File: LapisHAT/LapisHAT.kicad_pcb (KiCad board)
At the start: 4 copper layers, 53 parts, among them J1 Conn_01x02, J10 Conn_01x02, J11 Conn_01x02, J12 Conn_01x02, J13 Conn_01x03, J14 Conn_01x03, J15 Conn_01x03, J16 Conn_01x03, J17 Conn_01x02, J18 Conn_01x02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

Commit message: Initial schematic
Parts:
- added C18: 47u, Capacitor_SMD:C_0805_2012Metric, F.Cu at (61.5, 39.4)
- added C19: 100n, Capacitor_SMD:C_0603_1608Metric, F.Cu at (66.2, 39.6)
- added C20: 100n, Capacitor_SMD:C_0603_1608Metric, F.Cu at (63.4, 39.6)
- added C21: 47u, Capacitor_SMD:C_0805_2012Metric, F.Cu at (66.2, 32.5)
- added C22: 100n, Capacitor_SMD:C_0603_1608Metric, F.Cu at (71.1, 32.5)
- added C23: 100n, Capacitor_SMD:C_0603_1608Metric, F.Cu at (69.4, 32.5)
- added J19: Conn_01x02, Connector_PinHeader_2.54mm:PinHeader_1x02_P2.54mm_Vertical, F.Cu at (59.9, 32.4)
- added R7: 10k, Resistor_SMD:R_0603_1608Metric, F.Cu at (65.4, 46.7)
- added R8: 10k, Resistor_SMD:R_0603_1608Metric, F.Cu at (71.0, 39.8)
- added U10: DRV8231ADSG, Package_SON:WSON-8-1EP_2x2mm_P0.5mm_EP0.9x1.6mm, F.Cu at (65.2, 43.2)
- added U11: DRV8231ADSG, Package_SON:WSON-8-1EP_2x2mm_P0.5mm_EP0.9x1.6mm, F.Cu at (70.9, 36.3)
- J2: moved to B.Cu
- J3, J4: value Conn_01x07 -> Conn_01x06; footprint Connector_PinHeader_2.54mm:PinHeader_1x07_P2.54mm_Vertical -> Connector_PinHeader_2.54mm:PinHeader_1x06_P2.54mm_Vertical
- moved C8 174.8 mm to (61.5, 58.1), turned to 180 degrees
- moved J18 173.9 mm to (59.3, 72.7), turned to 90 degrees
- moved U6 170.8 mm to (66.0, 61.4), turned to 180 degrees
- moved Q1 169.1 mm to (65.8, 68.4), turned to 180 degrees
- moved Q2 169.0 mm to (65.9, 72.7), turned to 180 degrees
- moved J17 168.8 mm to (59.2, 68.4), turned to 90 degrees
- moved C5 168.3 mm to (67.9, 49.1), turned to 90 degrees
- moved C10 166.1 mm to (64.8, 57.5), turned to 90 degrees
- moved U4 165.9 mm to (70.5, 52.8), turned to 180 degrees
- moved R2 164.7 mm to (66.2, 63.5), turned to 180 degrees
- moved C9 164.3 mm to (66.5, 57.6), turned to 90 degrees
- moved J4 163.5 mm to (54.6, 47.4)
- moved J9 163.4 mm to (72.5, 79.8), turned to 90 degrees
- moved C7 162.4 mm to (68.2, 58.1), turned to 90 degrees
- moved C2 161.2 mm to (67.8, 39.6), turned to 90 degrees
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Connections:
- net Net-(J5-Pin_1) renamed /Tooling/MOTOR2_OUT1
- net Net-(J5-Pin_2) renamed /Tooling/MOTOR2_OUT2
- net Net-(J6-Pin_1) renamed /Tooling/MOTOR3_OUT1
- net Net-(J6-Pin_2) renamed /Tooling/MOTOR3_OUT2
- A1 pad 1: /Pico/MOTOR0_PWM -> /Pico/MOTOR0_DIR
- A1 pad 10: /Pico/ESC3 -> /Pico/MOTOR3_PWM
- A1 pad 11: /Pico/ESC4 -> /Pico/LED0
- A1 pad 12: /Pico/ESC5 -> /Pico/LED1
- A1 pad 14: /Pico/SERVO0 -> /Pico/ESC0
- A1 pad 15: /Pico/SERVO1 -> /Pico/ESC1
- A1 pad 16: /Pico/SERVO2 -> /Pico/ESC2
- A1 pad 17: /Pico/SERVO3 -> /Pico/ESC3
- A1 pad 19: /Pico/LED0 -> /Pico/ESC4
- A1 pad 2: /Pico/MOTOR0_DIR -> /Pico/MOTOR1_DIR
- A1 pad 20: /Pico/LED1 -> /Pico/ESC5
- A1 pad 21: /Pico/MOTOR2_DIR -> /Pico/SERVO0
- A1 pad 22: /Pico/MOTOR2_PWM -> /Pico/SERVO1
- A1 pad 24: /Pico/MOTOR1_PWM -> /Pico/SERVO2
- A1 pad 25: /Pico/MOTOR1_DIR -> /Pico/SERVO3
- A1 pad 4: /Pico/MOTOR3_DIR -> /Pico/MOTOR2_DIR
- A1 pad 5: /Pico/MOTOR3_PWM -> /Pico/MOTOR3_DIR
- A1 pad 6: /Pico/ESC0 -> /Pico/MOTOR0_PWM
- A1 pad 7: /Pico/ESC1 -> /Pico/MOTOR1_PWM
- A1 pad 9: /Pico/ESC2 -> /Pico/MOTOR2_PWM
- J3 pad 1: +12V -> +3V3
- J3 pad 2: +3V3 -> /Tooling/MOTOR0_OUT1
- J3 pad 3: Net-(J3-Pin_3) -> /Tooling/MOTOR0_OUT2
- J3 pad 4: Net-(J3-Pin_4) -> /I2C/ENCODER0_SDA
- J3 pad 5: /I2C/ENCODER0_SDA -> /I2C/ENCODER0_SCL
- J3 pad 6: /I2C/ENCODER0_SCL -> GND
- J4 pad 1: +12V -> +3V3
- J4 pad 2: +3V3 -> /Tooling/MOTOR1_OUT1
- J4 pad 3: Net-(J4-Pin_3) -> /Tooling/MOTOR1_OUT2
- J4 pad 4: Net-(J4-Pin_4) -> /I2C/ENCODER1_SDA
- J4 pad 5: /I2C/ENCODER1_SDA -> /I2C/ENCODER1_SCL
- J4 pad 6: /I2C/ENCODER1_SCL -> GND
- U1 pad 4: Net-(J3-Pin_4) -> Net-(U1-Y1)
- U1 pad 6: Net-(J3-Pin_3) -> Net-(U1-Y0)
- U2 pad 4: Net-(J4-Pin_4) -> Net-(U10-IN2)
- U2 pad 6: Net-(J4-Pin_3) -> Net-(U10-IN1)
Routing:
- net /I2C/ENCODER0_SCL: track 0.00 -> 75.0 mm, vias 0 -> 1
- net /I2C/ENCODER0_SDA: track 0.00 -> 71.6 mm, vias 0 -> 2
- net /I2C/ENCODER1_SCL: track 0.00 -> 69.4 mm, vias 0 -> 2
- net /I2C/ENCODER1_SDA: track 0.00 -> 66.3 mm, vias 0 -> 1
- net +3V3: track 0.00 -> 39.7 mm, vias 0 -> 13
- net +5V: track 0.00 -> 29.8 mm
- net /I2C/ENCODER_SDA: track 0.00 -> 24.3 mm
- net +12V: track 0.00 -> 23.6 mm, vias 0 -> 12
- net /I2C/ENCODER_SCL: track 0.00 -> 23.2 mm
- net GND: track 0.00 -> 20.1 mm, vias 0 -> 16
- net /Pico/MOTOR3_DIR: track 0.00 -> 19.7 mm
- net /Pico/MOTOR0_PWM: track 0.00 -> 18.3 mm, vias 0 -> 1
- net /Pico/LED1: track 0.00 -> 18.3 mm
- net /Pico/LED0: track 0.00 -> 17.5 mm
- net /Pico/MOTOR1_PWM: track 0.00 -> 16.7 mm, vias 0 -> 1
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- added copper zone on In2.Cu, net +12V
- added copper zone on In1.Cu, net +3V3
- added copper zone on In1.Cu, net +5V
- added copper zone on In1.Cu, net /Tooling/MOTOR0_OUT1
- added copper zone on In1.Cu, net /Tooling/MOTOR0_OUT2
- added copper zone on In1.Cu, net /Tooling/MOTOR1_OUT1
- added copper zone on In1.Cu, net /Tooling/MOTOR1_OUT2
- added copper zone on In1.Cu, net /Tooling/MOTOR2_OUT1
- added copper zone on In1.Cu, net /Tooling/MOTOR2_OUT2
- added copper zone on In1.Cu, net /Tooling/MOTOR3_OUT1
- added copper zone on In1.Cu, net /Tooling/MOTOR3_OUT2
- added copper zone on B.Cu, net GND
- added copper zone on F.Cu, net GND

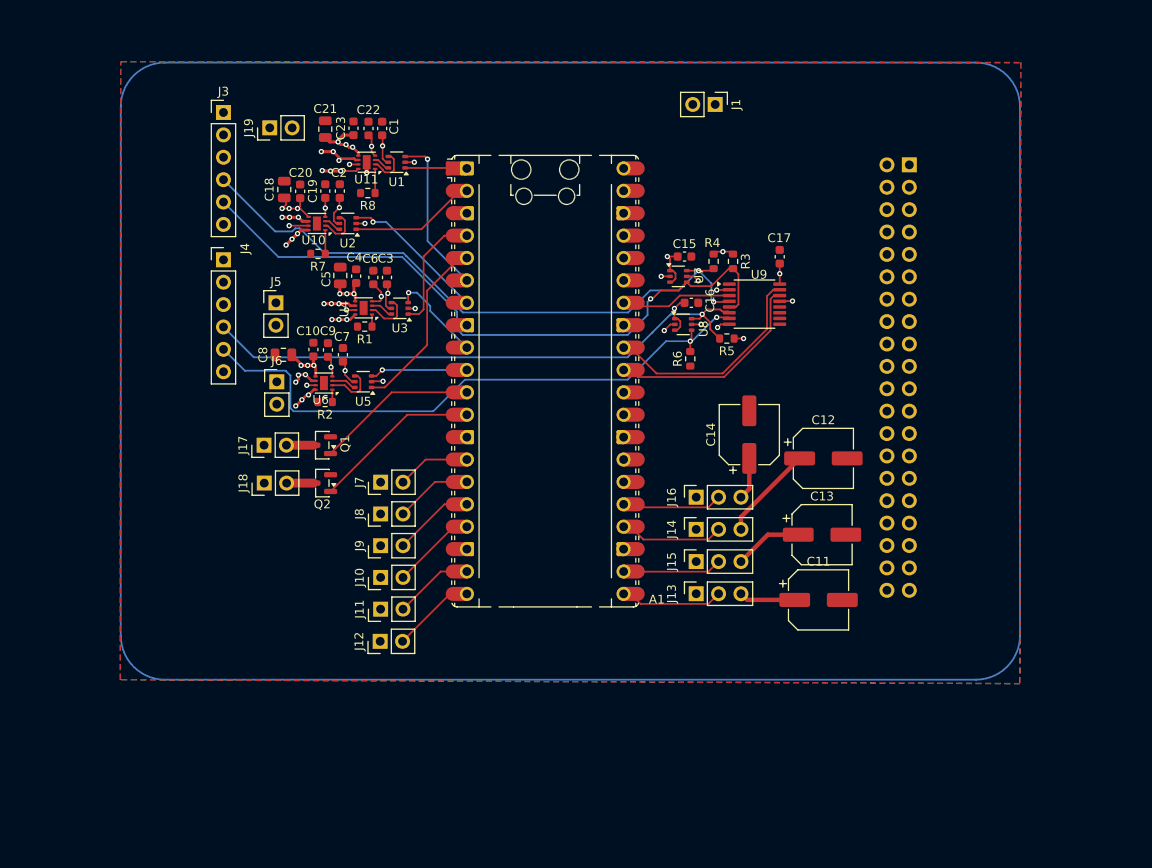
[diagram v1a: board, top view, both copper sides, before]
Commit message: New Lapis Hat
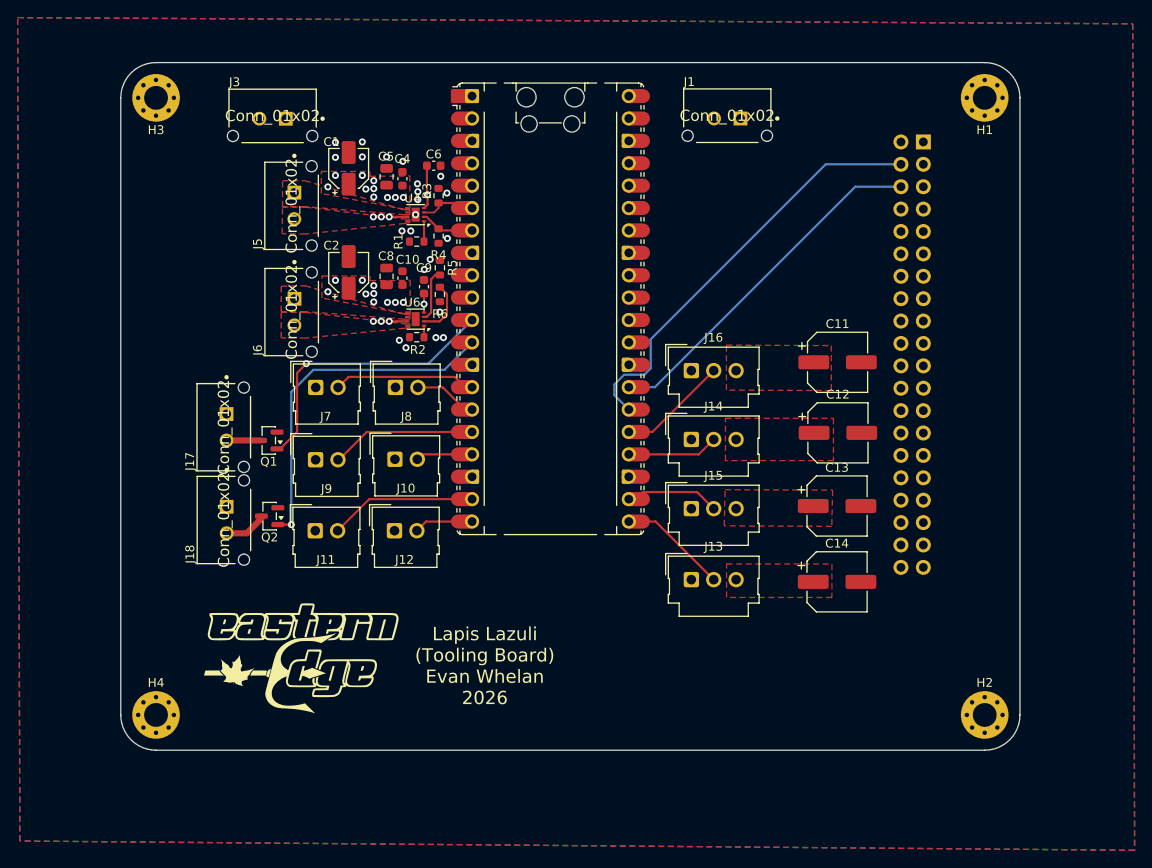
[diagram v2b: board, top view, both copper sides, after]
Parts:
- removed C15, C16: 10n, Capacitor_SMD:C_0603_1608Metric
- removed C17, C19, C20, C22, C23, C3, C7: 100n, Capacitor_SMD:C_0603_1608Metric
- removed C18, C21: 47u, Capacitor_SMD:C_0805_2012Metric
- removed J19: Conn_01x02, Connector_PinHeader_2.54mm:PinHeader_1x02_P2.54mm_Vertical
- removed J4: Conn_01x06, Connector_PinHeader_2.54mm:PinHeader_1x06_P2.54mm_Vertical
- removed R7, R8: 10k, Resistor_SMD:R_0603_1608Metric
- removed U1, U2, U3, U5: NC7SZ18P6X, Package_TO_SOT_SMD:SOT-363_SC-70-6
- removed U10, U11: DRV8231ADSG, Package_SON:WSON-8-1EP_2x2mm_P0.5mm_EP0.9x1.6mm
- removed U7, U8: LTC4311CSC6-TRPBF, Package_TO_SOT_SMD:SOT-363_SC-70-6
- removed U9: TCA9546APW, Package_SO:TSSOP-16_4.4x5mm_P0.65mm
- added G***: LOGO, EER_Logos:eer_logo_small, F.Cu at (63.5, 91.3)
- added H1: MountingHole_Pad, MountingHole:MountingHole_2.7mm_M2.5_Pad_Via, F.Cu at (141.0, 29.0)
- added H2: MountingHole_Pad, MountingHole:MountingHole_2.7mm_M2.5_Pad_Via, F.Cu at (141.0, 99.0)
- added H3: MountingHole_Pad, MountingHole:MountingHole_2.7mm_M2.5_Pad_Via, F.Cu at (47.0, 29.0)
- added H4: MountingHole_Pad, MountingHole:MountingHole_2.7mm_M2.5_Pad_Via, F.Cu at (47.0, 99.0)
- C1, C2: value 100n -> 10u; footprint Capacitor_SMD:C_0603_1608Metric -> Capacitor_SMD:CP_Elec_4x5.4
- J1, J17, J18, J5, J6: footprint Connector_PinHeader_2.54mm:PinHeader_1x02_P2.54mm_Vertical -> footprints:Molex-43650-0227_-MFG
- J10, J11, J12, J7, J8, J9: footprint Connector_PinHeader_2.54mm:PinHeader_1x02_P2.54mm_Vertical -> Connector_Molex:Molex_SL_171971-0002_1x02_P2.54mm_Vertical
- J13, J14, J15, J16: footprint Connector_PinSocket_2.54mm:PinSocket_1x03_P2.54mm_Vertical -> Connector_Molex:Molex_SL_171971-0003_1x03_P2.54mm_Vertical
- J3: value Conn_01x06 -> Conn_01x02; footprint Connector_PinHeader_2.54mm:PinHeader_1x06_P2.54mm_Vertical -> footprints:Molex-43650-0227_-MFG
- moved R3 34.2 mm to (79.0, 40.1)
- moved R5 33.5 mm to (79.2, 48.3), turned to -90 degrees
- moved R4 31.3 mm to (79.0, 44.7), turned to 90 degrees
- moved R6 29.3 mm to (79.2, 51.3)
- moved C11 27.0 mm to (124.3, 59.0)
- moved C14 19.4 mm to (124.2, 83.9), turned to 0 degrees
- moved C8 14.7 mm to (73.2, 49.2), turned to 90 degrees
- moved J8 14.4 mm to (74.2, 61.9), turned to 0 degrees
- moved C6 14.4 mm to (78.5, 36.7), turned to 0 degrees
- moved J16 14.4 mm to (107.7, 59.9), turned to 0 degrees
- moved J10 13.5 mm to (74.1, 70.0), turned to 0 degrees
- moved C9 13.0 mm to (77.4, 50.4)
- moved J7 13.0 mm to (65.1, 61.9), turned to 0 degrees
- moved C10 12.9 mm to (75.0, 49.5)
- moved R2 12.7 mm to (76.6, 56.1)
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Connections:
- A1 pad 1: /Pico/MOTOR0_DIR -> unconnected-(A1-GPIO0-Pad1)
- A1 pad 10: /Pico/MOTOR3_PWM -> /Pico/MOTOR1_IN2
- A1 pad 2: /Pico/MOTOR1_DIR -> unconnected-(A1-GPIO1-Pad2)
- A1 pad 31: /I2C/ENCODER_SCL -> unconnected-(A1-GPIO26_ADC0-Pad31)_1
- A1 pad 32: /I2C/ENCODER_SDA -> unconnected-(A1-GPIO27_ADC1-Pad32)
- A1 pad 34: /I2C/~{I2C_MUX_RESET} -> unconnected-(A1-GPIO28_ADC2-Pad34)
- A1 pad 4: /Pico/MOTOR2_DIR -> unconnected-(A1-GPIO2-Pad4)_1
- A1 pad 5: /Pico/MOTOR3_DIR -> unconnected-(A1-GPIO3-Pad5)_1
- A1 pad 6: /Pico/MOTOR0_PWM -> /Pico/MOTOR0_IN1
- A1 pad 7: /Pico/MOTOR1_PWM -> /Pico/MOTOR0_IN2
- A1 pad 9: /Pico/MOTOR2_PWM -> /Pico/MOTOR1_IN1
- C1 pad 1: +3V3 -> +12V
- C2 pad 1: +3V3 -> +12V
- J3 pad 1: +3V3 -> GND
- J3 pad 2: /Tooling/MOTOR0_OUT1 -> +12V
- J5 pad 1: /Tooling/MOTOR2_OUT1 -> /Tooling/MOTOR0_OUT1
- J5 pad 2: /Tooling/MOTOR2_OUT2 -> /Tooling/MOTOR0_OUT2
- J6 pad 1: /Tooling/MOTOR3_OUT1 -> /Tooling/MOTOR0_OUT1
- J6 pad 2: /Tooling/MOTOR3_OUT2 -> /Tooling/MOTOR0_OUT2
- R3 pad 1: +3V3 -> GND
- R3 pad 2: /I2C/ENCODER0_SCL -> /Pico/MOTOR0_IN1
- R4 pad 1: +3V3 -> GND
- R4 pad 2: /I2C/ENCODER0_SDA -> /Pico/MOTOR0_IN2
- R5 pad 1: +3V3 -> GND
- R5 pad 2: /I2C/ENCODER1_SDA -> /Pico/MOTOR1_IN1
- R6 pad 1: +3V3 -> GND
- R6 pad 2: /I2C/ENCODER1_SCL -> /Pico/MOTOR1_IN2
- U4 pad 2: Net-(U3-Y1) -> /Pico/MOTOR0_IN2
- U4 pad 3: Net-(U3-Y0) -> /Pico/MOTOR0_IN1
- U4 pad 6: /Tooling/MOTOR2_OUT1 -> /Tooling/MOTOR0_OUT1
- U4 pad 8: /Tooling/MOTOR2_OUT2 -> /Tooling/MOTOR0_OUT2
- U6 pad 2: Net-(U5-Y1) -> /Pico/MOTOR1_IN2
- U6 pad 3: Net-(U5-Y0) -> /Pico/MOTOR1_IN1
- U6 pad 6: /Tooling/MOTOR3_OUT1 -> /Tooling/MOTOR0_OUT1
- U6 pad 8: /Tooling/MOTOR3_OUT2 -> /Tooling/MOTOR0_OUT2
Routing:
- net /I2C/ENCODER0_SCL: track 75.0 -> 0.00 mm, vias 1 -> 0
- net /I2C/ENCODER0_SDA: track 71.6 -> 0.00 mm, vias 2 -> 0
- net /I2C/ENCODER1_SCL: track 69.4 -> 0.00 mm, vias 2 -> 0
- net /I2C/ENCODER1_SDA: track 66.3 -> 0.00 mm, vias 1 -> 0
- net /Pico/PI_SDA: track 0.00 -> 48.7 mm
- net /Pico/PI_SCL: track 0.00 -> 40.3 mm
- net +3V3: track 39.7 -> 7.15 mm, vias 13 -> 2
- net +5V: track 29.8 -> 0.00 mm
- net /I2C/ENCODER_SDA: track 24.3 -> 0.00 mm
- net +12V: track 23.6 -> 0.00 mm, vias 12 -> 20
- net /I2C/ENCODER_SCL: track 23.2 -> 0.00 mm
- net /Pico/LED1: track 18.3 -> 39.4 mm, vias 0 -> 1
- net /Pico/MOTOR3_DIR: track 19.7 -> 0.00 mm
- net /Pico/MOTOR0_PWM: track 18.3 -> 0.00 mm, vias 1 -> 0
- net /Pico/MOTOR1_PWM: track 16.7 -> 0.00 mm, vias 1 -> 0
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- added copper zone on F.Cu, net +12V
- added copper zone on F.Cu, net +5V
- added copper zone on F.Cu, net /Tooling/MOTOR0_OUT1
- added copper zone on F.Cu, net /Tooling/MOTOR0_OUT2
- removed copper zone on In1.Cu, net /Tooling/MOTOR0_OUT1
- removed copper zone on In1.Cu, net /Tooling/MOTOR0_OUT2
- removed copper zone on In1.Cu, net /Tooling/MOTOR1_OUT1
- removed copper zone on In1.Cu, net /Tooling/MOTOR1_OUT2
- removed copper zone on In1.Cu, net /Tooling/MOTOR2_OUT1
- removed copper zone on In1.Cu, net /Tooling/MOTOR2_OUT2
- removed copper zone on In1.Cu, net /Tooling/MOTOR3_OUT1
- removed copper zone on In1.Cu, net /Tooling/MOTOR3_OUT2
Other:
- board outline added: 102 x 78 mm
- board text added: "Lapis Lazuli (Tooling Board) Evan Whelan 2026"

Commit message: Some review changes
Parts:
- added C3: 100u, Capacitor_SMD:CP_Elec_6.3x7.7, F.Cu at (170.2, 61.3)
- added D1: LED, LED_SMD:LED_0603_1608Metric, F.Cu at (118.8, 39.0)
- added D2: LED, LED_SMD:LED_0603_1608Metric, F.Cu at (112.5, 50.0)
- added D3: LED, LED_SMD:LED_0603_1608Metric, F.Cu at (53.5, 46.0)
- added R10: 4.7k, Resistor_SMD:R_0603_1608Metric, F.Cu at (167.0, 66.6)
- added R11: 4.7k, Resistor_SMD:R_0603_1608Metric, F.Cu at (167.0, 69.2)
- added R7: 100, Resistor_SMD:R_0603_1608Metric, F.Cu at (108.3, 39.0)
- added R8: 330, Resistor_SMD:R_0603_1608Metric, F.Cu at (119.5, 50.0)
- added R9: 2k, Resistor_SMD:R_0603_1608Metric, F.Cu at (53.5, 39.8)
- added TP1: TestPoint, TestPoint:TestPoint_Pad_2.0x2.0mm, F.Cu at (48.0, 47.2)
- added TP2: TestPoint, TestPoint:TestPoint_Pad_2.0x2.0mm, F.Cu at (122.8, 31.2)
- added TP4: TestPoint, TestPoint:TestPoint_Pad_2.0x2.0mm, F.Cu at (52.0, 55.2)
- added TP5: TestPoint, TestPoint:TestPoint_Pad_2.0x2.0mm, F.Cu at (110.0, 43.8)
- added TP6: TestPoint, TestPoint:TestPoint_Pad_2.0x2.0mm, F.Cu at (105.8, 43.8)
- C1, C2: value 10u -> 330u
- H1, H2, H3, H4: footprint MountingHole:MountingHole_2.7mm_M2.5_Pad_Via -> MountingHole:MountingHole_3.2mm_M3_Pad_Via
- moved R1 103.7 mm to (179.4, 58.5), turned to 0 degrees
- moved R2 103.0 mm to (179.4, 61.0), turned to 0 degrees
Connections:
- J6 pad 1: /Tooling/MOTOR0_OUT1 -> /Tooling/MOTOR1_OUT1
- J6 pad 2: /Tooling/MOTOR0_OUT2 -> /Tooling/MOTOR1_OUT2
- R1 pad 1: Net-(U4-IPROPI) -> GND
- R1 pad 2: GND -> /Pico/LED0
- R2 pad 1: Net-(U6-IPROPI) -> GND
- R2 pad 2: GND -> /Pico/LED1
- U4 pad 1: Net-(U4-IPROPI) -> GND
- U6 pad 1: Net-(U6-IPROPI) -> GND
- U6 pad 6: /Tooling/MOTOR0_OUT1 -> /Tooling/MOTOR1_OUT1
- U6 pad 8: /Tooling/MOTOR0_OUT2 -> /Tooling/MOTOR1_OUT2
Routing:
- net /Pico/PI_SDA: track 48.7 -> 72.8 mm
- net /Pico/PI_SCL: track 40.3 -> 60.9 mm
- net Net-(D1-A): track 0.00 -> 8.81 mm
- net +3V3: track 7.15 -> 14.0 mm
- net Net-(D2-A): track 0.00 -> 5.39 mm
- net Net-(D3-A): track 0.00 -> 4.56 mm
- net +12V: track 0.00 -> 4.00 mm, vias 20 -> 22
- net +5V: track 0.00 -> 3.67 mm, vias 0 -> 2
- net /Pico/MOTOR1_IN2: track 6.32 -> 9.67 mm
- net /Pico/MOTOR1_IN1: track 5.98 -> 8.84 mm
- net GND: track 7.70 -> 10.5 mm
- net Net-(U4-IPROPI): track 2.25 -> 0.00 mm
- net Net-(U6-IPROPI): track 1.30 -> 0.00 mm
- added copper zone on F.Cu, net /Tooling/MOTOR1_OUT1
- added copper zone on F.Cu, net /Tooling/MOTOR1_OUT2

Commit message: another layout
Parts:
- removed A1: RaspberryPi_Pico, Module:RaspberryPi_Pico_Common_Unspecified
- removed G***: LOGO, EER_Logos:eer_logo_small
- removed R10, R11: 4.7k, Resistor_SMD:R_0603_1608Metric
- removed TP5, TP6: TestPoint, TestPoint:TestPoint_Pad_2.0x2.0mm
- added J19: Conn_01x20, Connector_PinHeader_2.54mm:PinHeader_1x20_P2.54mm_Vertical, B.Cu at (122.0, 44.6)
- added J4: Conn_01x20, Connector_PinHeader_2.54mm:PinHeader_1x20_P2.54mm_Vertical, B.Cu at (97.2, 44.8)
- added R12: 4.7k, Resistor_SMD:R_0603_1608Metric, F.Cu at (125.2, 57.5)
- added R13: 4.7k, Resistor_SMD:R_0603_1608Metric, F.Cu at (127.8, 57.5)
- H1, H2, H3, H4: footprint MountingHole:MountingHole_3.2mm_M3_Pad_Via -> MountingHole:MountingHole_2.7mm_M2.5_Pad_Via
- J1, J3: footprint footprints:Molex-43650-0227_-MFG -> Connector_Molex:Molex_Micro-Fit_3.0_43650-0200_1x02_P3.00mm_Horizontal
- J10, J11, J12, J7, J8, J9: footprint Connector_Molex:Molex_SL_171971-0002_1x02_P2.54mm_Vertical -> footprints:CONN_70553-xxxx_02_MOL
- J2: moved to F.Cu
- moved Q2 289.2 mm to (345.9, 119.3), turned to 0 degrees
- moved C1 163.5 mm to (223.8, 89.1), turned to 0 degrees
- moved U4 162.9 mm to (229.9, 97.0), turned to 0 degrees
- moved C2 161.7 mm to (223.8, 94.9), turned to 0 degrees
- moved U6 160.3 mm to (229.9, 100.6), turned to 0 degrees
- moved J17 151.2 mm to (205.5, 77.0), turned to 0 degrees
- moved J18 151.0 mm to (205.5, 84.3), turned to 0 degrees
- moved Q1 148.9 mm to (206.1, 95.7)
- moved R3 147.5 mm to (217.9, 89.9), turned to 0 degrees
- moved C4 147.4 mm to (213.9, 87.4), turned to 0 degrees
- moved R4 146.9 mm to (217.9, 92.4), turned to 0 degrees
- moved R5 146.4 mm to (217.9, 94.9), turned to 0 degrees
- moved C10 146.2 mm to (213.9, 94.9), turned to 0 degrees
- moved R6 146.2 mm to (217.9, 97.4), turned to 0 degrees
- moved C6 145.5 mm to (213.9, 89.9)
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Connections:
- C3 pad 2: unconnected-(C3-Pad2) -> GND
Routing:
- net /Pico/LED1: track 39.4 -> 0.00 mm, vias 1 -> 0
- net /Pico/ESC0: track 15.4 -> 51.8 mm
- net /Pico/ESC1: track 6.39 -> 41.2 mm
- net /Pico/LED0: track 32.1 -> 0.08 mm, vias 1 -> 0
- net /Pico/PI_SDA: track 72.8 -> 43.6 mm, vias 0 -> 1
- net /Pico/ESC3: track 5.73 -> 24.8 mm
- net /Pico/PI_SCL: track 60.9 -> 43.6 mm, vias 0 -> 1
- net /Pico/ESC2: track 15.7 -> 31.3 mm
- net /Pico/SERVO3: track 12.0 -> 23.3 mm
- net +3V3: track 14.0 -> 3.52 mm, vias 2 -> 3
- net /Pico/MOTOR1_IN2: track 9.67 -> 0.00 mm
- net /Pico/MOTOR1_IN1: track 8.84 -> 0.00 mm
- net /Pico/SERVO2: track 9.53 -> 17.8 mm
- net GND: track 10.5 -> 2.42 mm, vias 28 -> 2
- net /Pico/ESC5: track 5.87 -> 13.7 mm
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- added copper zone on In2.Cu, net GND
- removed copper zone on F.Cu, net +12V
- removed copper zone on In2.Cu, net +12V
- removed copper zone on F.Cu, net +5V
- removed copper zone on F.Cu, net /Tooling/MOTOR0_OUT1
- removed copper zone on F.Cu, net /Tooling/MOTOR0_OUT2
- removed copper zone on F.Cu, net /Tooling/MOTOR1_OUT1
- removed copper zone on F.Cu, net /Tooling/MOTOR1_OUT2
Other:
- board outline removed
- board text removed: "Lapis Lazuli (Tooling Board) Evan Whelan 2026"

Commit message: Move connectors and add correct 5v cap
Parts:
- C3: value 100u -> 120u; footprint Capacitor_SMD:CP_Elec_6.3x7.7 -> Capacitor_SMD:CP_Elec_10x12.5
- moved Q2 116.1 mm to (235.4, 83.7)
- moved J7 87.7 mm to (89.6, 32.0), turned to 180 degrees
- moved J12 84.5 mm to (137.4, 32.0), turned to 180 degrees
- moved J8 78.3 mm to (99.1, 32.0), turned to 180 degrees
- moved J11 76.2 mm to (127.7, 32.0), turned to 180 degrees
- moved J9 72.8 mm to (108.6, 32.0), turned to 180 degrees
- moved J10 72.0 mm to (118.1, 32.0), turned to 180 degrees
- moved J1 51.1 mm to (132.0, 99.0), turned to 180 degrees
- moved C3 48.3 mm to (117.5, 101.5), turned to 180 degrees
- moved D2 14.0 mm to (134.2, 47.5)
- moved R8 14.0 mm to (132.5, 47.5)
- moved J16 6.15 mm to (133.3, 61.0), turned to 180 degrees
- moved J15 5.30 mm to (133.3, 80.2), turned to 180 degrees
- moved J14 4.51 mm to (128.2, 67.5)
- moved D1 3.58 mm to (128.2, 48.6)
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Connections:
- J4 pad 10: /Pico/MOTOR1_IN2 -> /Pico/ESC3
- J4 pad 11: /Pico/LED0 -> /Pico/ESC4
- J4 pad 12: /Pico/LED1 -> /Pico/ESC5
- J4 pad 14: /Pico/ESC0 -> /Pico/MOTOR0_IN1
- J4 pad 15: /Pico/ESC1 -> /Pico/MOTOR0_IN2
- J4 pad 16: /Pico/ESC2 -> /Pico/MOTOR1_IN1
- J4 pad 17: /Pico/ESC3 -> /Pico/MOTOR1_IN2
- J4 pad 19: /Pico/ESC4 -> /Pico/LED0
- J4 pad 20: /Pico/ESC5 -> /Pico/LED1
- J4 pad 6: /Pico/MOTOR0_IN1 -> /Pico/ESC0
- J4 pad 7: /Pico/MOTOR0_IN2 -> /Pico/ESC1
- J4 pad 9: /Pico/MOTOR1_IN1 -> /Pico/ESC2
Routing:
- net /Pico/ESC5: track 13.7 -> 63.8 mm
- net /Pico/PI_SCL: track 43.6 -> 1.42 mm
- net /Pico/PI_SDA: track 43.6 -> 1.42 mm
- net /Pico/ESC4: track 15.1 -> 52.6 mm
- net /Pico/SERVO3: track 23.3 -> 0.00 mm
- net /Pico/ESC0: track 51.8 -> 29.8 mm
- net /Pico/ESC3: track 24.8 -> 46.1 mm
- net /Pico/SERVO2: track 17.8 -> 0.00 mm
- net /Pico/SERVO1: track 14.8 -> 0.00 mm
- net /Pico/SERVO0: track 12.5 -> 0.00 mm
- net /Pico/ESC2: track 31.3 -> 39.6 mm
- net /Pico/ESC1: track 41.2 -> 34.5 mm
- net +5V: track 6.78 -> 9.50 mm
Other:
- board text added: "${REFERENCE}"
